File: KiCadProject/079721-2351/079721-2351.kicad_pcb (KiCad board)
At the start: 2 copper layers, 159.3 x 154.2 mm, 241 parts, among them IC1 HC244, IC101 uPC177C, IC201 MP493, IC401 D151811-0360, IC402 IS157, IC501 D151821-0020, IC601 MP5273, IC602 TC4071BP_2, IC603 TC4069UPB_2, J201 Connected, J44 Conn_02x11_0x13_Top_Bottom_Sh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, J601 Connected, J711 Empty, Q802 C945, T1 2SB1015B, T211 RN1006, T711 2CS2001, T712 2SD1415, T721 2CS2001, T722 2SD1415, T751 CE1A3Q, T761 CE1A3Q, T801 2CS2001, T803 2CS4065, T811 2CS2001, T812 CE1A3Q, T821 Empty, T822 CE1A3Q (empty), T831 Empty, T832 CE1A3Q (empty), T841 2CS2001, T842 CE1A3Q, T851 Empty, T852 CE1A3Q (empty), T861 Empty, T911 RN1006, T921 RN1006, T921A1 Conn_01x01_Female, T921B1 Conn_01x01_Female, X601 Crystal

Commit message: Cleanup
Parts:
- removed IC602: TC4071BP_2, 40xx:40xx-DIL14
- removed IC603: TC4069UPB_2, 40xx:40xx-DIL14
- removed T712, T722: 2SD1415, 079721-2351:TO-220-3_Vertical_Mazda
- added T712A1: 2SD1415, 079721-2351:TO-220-3_Vertical_Mazda, F.Cu at (109.7, 29.0)
- added T722A1: 2SD1415, 079721-2351:TO-220-3_Vertical_Mazda, F.Cu at (125.5, 29.0)
- added U1: 4071, 40xx:40xx-DIL14, F.Cu at (216.9, 69.5)
- added U2: 4069, 40xx:40xx-DIL14, F.Cu at (201.2, 69.5)
- R602: value R_Network08_US_mazda -> R
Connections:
- net C711_2 renamed Net-(C711-Pad2)
- net C721_2 renamed Net-(C721-Pad1)
- net IC402_3 renamed IC601_41
- net IC602_13 renamed IC601_38
- net IC602_8 renamed IC601_37
- net IC603_5 renamed IC601_28
- net J19 renamed IC601_6
- net J23 renamed IC601_7
- net Net-(IC101-Pad1) renamed IC601_11
- net Net-(IC201-Pad17) renamed IC201_17
- net Net-(IC201-Pad18) renamed IC201_18
- net Net-(IC201-Pad19) renamed IC201_19
- net Net-(IC401-Pad21) renamed IC601_34
- net Net-(IC401-Pad22) renamed IC601_33
- net Net-(IC401-Pad23) renamed IC601_32
- net Net-(IC501-Pad10) renamed IC601_16
- net Net-(IC501-Pad4) renamed IC601_14
- net Net-(IC501-Pad5) renamed IC601_15
- net Net-(IC501-Pad6) renamed IC601_12
- net Net-(IC601-Pad19) renamed IC601_19
- net Net-(IC601-Pad29) renamed IC601_29
- net Net-(IC601-Pad40) renamed IC601_40
- net Net-(IC601-Pad42) renamed IC601_42
- net T211_2 renamed IC601_8
- net T711_2 renamed Net-(R711-Pad1)
- net T721_2 renamed Net-(R721-Pad1)
- net T861_10 renamed IC601_10
- net T861_3 renamed IC601_5
- net T861_9 renamed IC601_9
- IC601 pad 13: T861_13 -> IC601_13
- IC601 pad 17: T861_17 -> IC601_17
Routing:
- net T861_17: track 74.9 -> 0.00 mm
- net IC601_17: track 0.00 -> 74.9 mm
- net T861_13: track 58.7 -> 0.00 mm
- net IC601_13: track 0.00 -> 58.7 mm

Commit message: Cleanup
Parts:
- T811: value 2CS2001 -> 2SC1815
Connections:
- net C504 renamed Net-(C504-Pad2)
- net IC101_11 renamed Net-(IC101-Pad11)
- net IC101_4 renamed Net-(IC101-Pad4)
- net IC101_7 renamed Net-(C503-Pad2)
- net IC1_5 renamed IC601_1
- net J22 renamed Net-(T851-Pad3)
- net Q802_2 renamed Net-(Q802-Pad2)
- net T211_3 renamed Net-(D211-Pad1)
- net T801_2 renamed Net-(R801-Pad1)
- net T803_1 renamed Net-(Q802-Pad1)
- net T803_3 renamed Net-(R804-Pad1)
- net T811_2 renamed Net-(R811-Pad1)
- net T812_2 renamed Net-(D812-Pad2)
- net T821_2 renamed Net-(R821-Pad1)
- net T831_2 renamed Net-(R831-Pad1)
- net T841_2 renamed Net-(R841-Pad1)
- net T842_2 renamed Net-(R842-Pad1)
- net T842_3 renamed Net-(R841-Pad2)
- net T851_2 renamed Net-(R851-Pad1)
- net T852_2 renamed Net-(D851-Pad2)
- net T852_3 renamed Net-(R851-Pad2)
- net T861_2 renamed Net-(R861-Pad1)
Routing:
- net Net-(Q802-Pad1): track 54.1 -> 55.3 mm
- net IC601_2: track 82.2 -> 83.3 mm

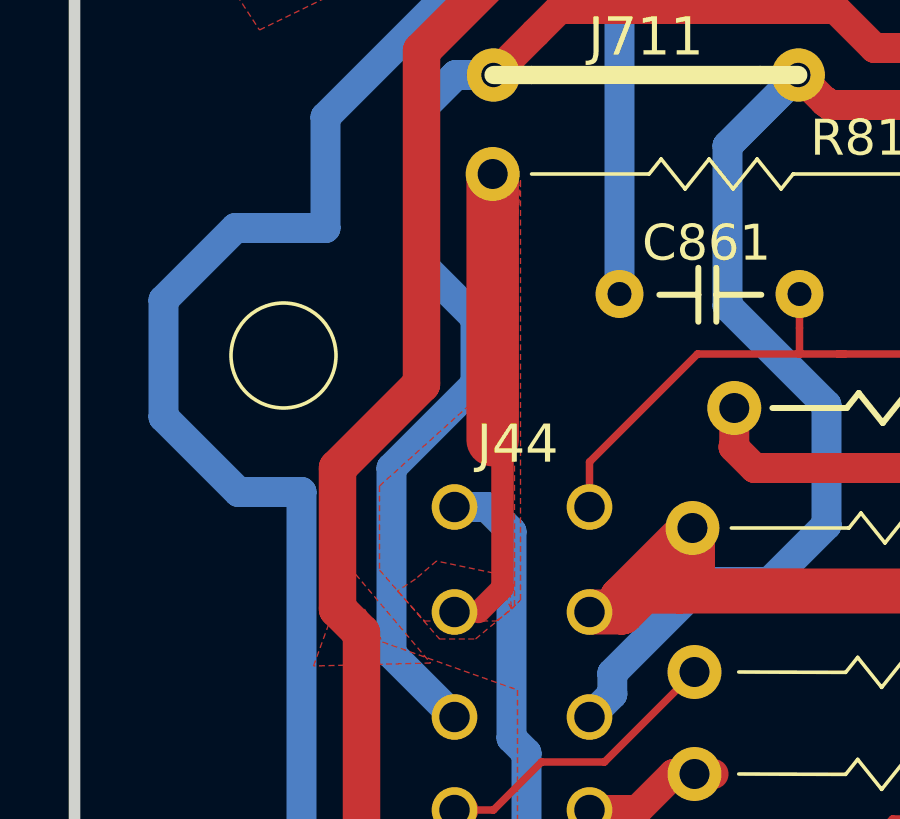
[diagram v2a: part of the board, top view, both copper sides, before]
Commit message: Input description TODO: Correct transistors pins
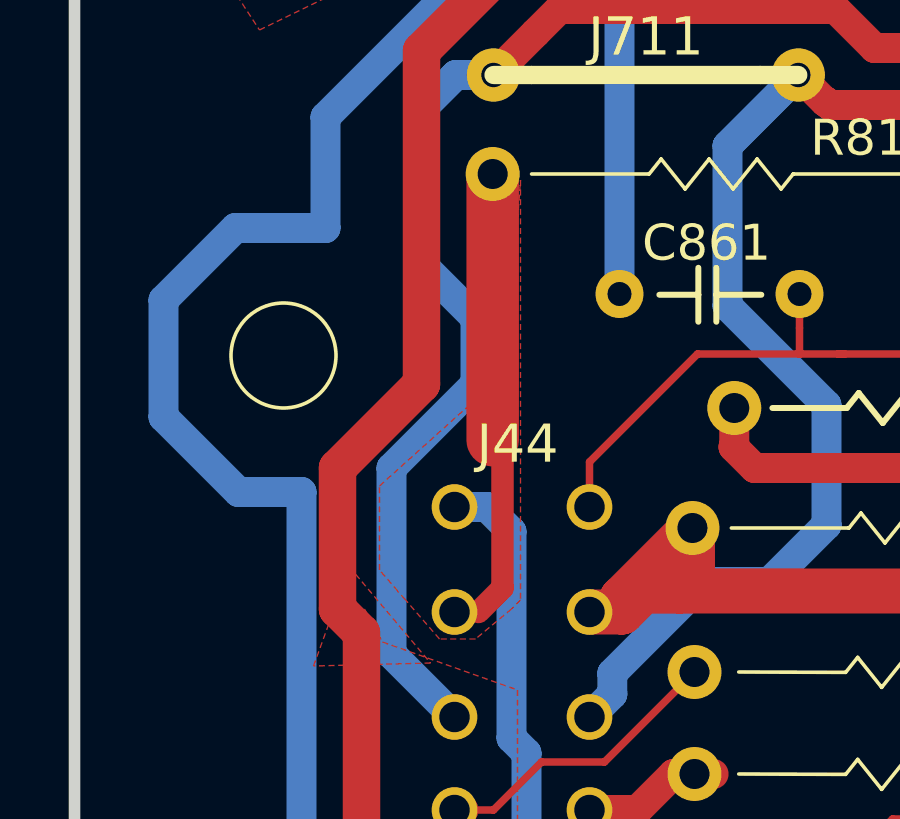
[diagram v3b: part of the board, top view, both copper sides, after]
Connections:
- net 2E renamed Crank_angle_sensor_N_CPK
- net 2G renamed Crank_angle_sensor_G_CMP
- net 2H renamed Fuel_pressure_regulator_solenoid_high_temp
- net 2I renamed Igniter_E
- net 2J renamed Radiator_fun_temperature_sensor
- net 2K renamed Airflow_meter_5V
- net 2L renamed Throttle_wide_open_sensor
- net 2M renamed Throttle_position_sensor
- net 2N renamed Oxygen_sensor
- net 2O renamed Volume_airflow_sensor
- net 2P renamed Airflow_meter_intake_air_thermosensor
- net 2Q renamed R432
- net 2U renamed Injectors_1_3
- net 2V renamed Injectors_2_4
- net 2W renamed Idle_air_control_valve
- net 2X renamed EVAP_canister_purage_valve
- net 2Z renamed Transsmision_control_module
- net A renamed +BATT
- net C renamed Starter_motor
- net D renamed Self_diagnostic_checker_monitor_lamp
- net E renamed Check_engine_indicator
- net F renamed Self_diagnostic_checker_code_no
- net G renamed Ignition_amp_1&4
- net H renamed Ignition_amp_2&3
- net J renamed AC_relay
- net L renamed Vehicle_speed_sensor
- net N renamed Throttle_sensor_idle_terminal
- net O renamed Stoplight_switch
- net P renamed Power_steering_pressure_switch
- net Q renamed AC_switch
- net R renamed Radiator_temperature_switch
- net S renamed Blower_motor_switch
- net U renamed Headlight_switch
- net V renamed Neutral_or_clutch_switch
- C1 pad 2: GND -> GNDS
- C101 pad 1: GND -> GNDS
- C105 pad 1: GND -> GNDS
- C111 pad 2: GND -> GNDS
- C2 pad 2: GND -> GNDS
- C201 pad 1: GND -> GNDS
- C202 pad 1: GND -> GNDS
- C203 pad 1: GND -> GNDS
- C204 pad 1: GND -> GNDS
- C205 pad 1: GND -> GNDS
- C3 pad 2: GND -> GNDS
- C4 pad 2: GND -> GNDS
- C401 pad 1: GND -> GNDS
- C405 pad 2: GND -> GNDS
- C411 pad 2: GND -> GNDS
- C421 pad 1: GND -> GNDS
- C422 pad 2: GND -> GNDS
- C431 pad 1: GND -> GNDS
- C432 pad 2: GND -> GNDS
- C441 pad 1: GND -> GNDS
- C442 pad 1: GND -> GNDS
- C451 pad 2: GND -> GNDS
- C452 pad 2: GND -> GNDS
- C461 pad 1: GND -> GNDS
- C471 pad 2: GND -> GNDS
- C472 pad 1: GND -> GNDS
- C481 pad 1: GND -> GNDS
- C491 pad 1: GND -> GNDS
- C5 pad 2: GND -> GNDS
- C501 pad 1: GND -> GNDS
- C502 pad 1: GND -> GNDS
- C503 pad 1: GND -> GNDS
- C504 pad 1: GND -> GNDS
- C51 pad 1: GND -> GNDS
- C511 pad 2: GND -> GNDS
- C52 pad 2: GND -> GNDS
- C53 pad 1: GND -> GNDS
- C54 pad 1: GND -> GNDS
- C6 pad 2: GND -> GNDS
- C601 pad 1: GND -> GNDS
- C602 pad 1: GND -> GNDS
- C603 pad 1: GND -> GNDS
- C604 pad 2: GND -> GNDS
- C605 pad 2: GND -> GNDS
- C606 pad 1: GND -> GNDS
- C607 pad 2: GND -> GNDS
- C7 pad 2: GND -> GNDS
- C8 pad 2: GND -> GNDS
- C801 pad 2: 2A -> GND
- C861 pad 2: GND -> GNDS
- C911 pad 2: GND -> GNDS
- C921 pad 2: GND -> GNDS
- D2 pad 2: GND -> GNDS
- D4 pad 2: GND -> GNDS
- D5 pad 2: GND -> GNDS
- D901 pad 1: 2A -> GND
- D901 pad 2: GND -> GNDS
- F401 pad 2: GND -> GNDS
- GND1 pad 1: GND -> GNDS
- IC1 pad 10: GND -> GNDS
- IC1 pad 9: GND -> GNDS
- IC101 pad 12: GND -> GNDS
- IC201 pad 12: GND -> GNDS
- IC401 pad 18: GND -> GNDS
- IC401 pad 25: GND -> GNDS
- IC401 pad 27: GND -> GNDS
- IC401 pad 28: GND -> GNDS
- IC402 pad 5: GND -> GNDS
- IC501 pad 12: GND -> GNDS
- IC601 pad 23: GND -> GNDS
- J201 pad 2: GND -> GNDS
- J44 pad 2A: 2A -> GND
- J44 pad 2B: 2A -> GND
- J44 pad 2C: GND -> GNDS
- J44 pad 2D: GND -> GNDS
- R104 pad 1: GND -> GNDS
- R114 pad 2: GND -> GNDS
- R401 pad 2: GND -> GNDS
- R412 pad 2: GND -> GNDS
- R451 pad 2: GND -> GNDS
- R463 pad 2: GND -> GNDS
- R483 pad 1: GND -> GNDS
- R493 pad 2: GND -> GNDS
- R502 pad 1: GND -> GNDS
- R507 pad 1: GND -> GNDS
- R508 pad 1: GND -> GNDS
- R509 pad 1: GND -> GNDS
- R562 pad 1: GND -> GNDS
- R712 pad 1: 2A -> GND
- R713 pad 2: 2A -> GND
- R722 pad 2: 2A -> GND
- R723 pad 2: 2A -> GND
- R805 pad 2: 2A -> GND
- T211 pad 1: GND -> GNDS
- T712A1 pad 3: 2A -> GND
- T722A1 pad 3: 2A -> GND
- T751 pad 1: GND -> GNDS
- T761 pad 1: GND -> GNDS
- T812 pad 1: 2A -> GND
- T822 pad 1: 2A -> GND
- T832 pad 1: 2A -> GND
- T842 pad 1: 2A -> GND
- T852 pad 1: 2A -> GND
- T861 pad 1: GND -> GNDS
- T911 pad 1: GND -> GNDS
- T921 pad 1: GND -> GNDS
- T921A1 pad 1: 2A -> GND
- U1 pad 7: GND -> GNDS
- U2 pad 7: GND -> GNDS
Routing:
- net GNDS: track 0.00 -> 1878.4 mm, vias 0 -> 11
- net GND: track 1878.4 -> 314.8 mm, vias 11 -> 1
- net 2A: track 314.8 -> 0.00 mm, vias 1 -> 0
- added copper zone on B.Cu, net GNDS
- added copper zone on F.Cu, net GNDS
- removed copper zone on B.Cu, net GND
- removed copper zone on F.Cu, net GND

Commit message: Cleanup
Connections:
- net IC402_24 renamed IC401_24
- net Net-(C491-Pad2) renamed IC401_19
- net Vehicle_speed_sensor renamed Transsmision_control_module_2

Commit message: Cleanup
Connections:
- net C501_2 renamed /IC501_20
- net C501_3 renamed /IC501_19
- net C501_5 renamed /IC501_17
- net C501_7 renamed /IC501_14
- net C502_7 renamed /IC501_13
- net IC101_2 renamed IC401_6
- net IC1_4 renamed +5V
- net IC201_15 renamed /IC201_15
- net IC201_16 renamed /IC201_16
- net IC201_18 renamed /IC201_18
- net IC201_19 renamed /IC201_19
- net IC401_19 renamed /IC401_19
- net IC402_4 renamed IC401_4
- net IC501_21 renamed /IC501_21
- net IC501_22 renamed /IC501_22
- net IC601_13 renamed /IC601_13
- net IC601_17 renamed /IC601_17
- net IC601_2 renamed /IC601_2
- net IC601_3 renamed /IC601_3
- net IC601_30 renamed /IC601_30
- net IC601_35 renamed /IC601_35
- net IC601_4 renamed /IC601_4
- net IC601_9 renamed /IC601_9
- net IC602_9 renamed Net-(U1-Pad12)
- net Net-(C201-Pad2) renamed /IC201_8
- net Net-(C202-Pad2) renamed /IC201_9
- net Net-(C203-Pad2) renamed /IC201_10
- net Net-(C204-Pad2) renamed /IC201_11
- net Net-(C401-Pad2) renamed /IC401_14
- net Net-(C422-Pad1) renamed /IC401_12
- net Net-(C432-Pad1) renamed /IC401_11
- net Net-(C442-Pad2) renamed /IC401_10
- net Net-(C452-Pad1) renamed /IC401_9
- net Net-(C472-Pad2) renamed /IC401_7
- net Net-(C481-Pad2) renamed /IC401_1
- net Net-(C501-Pad4) renamed /IC501_18
- net Net-(C501-Pad6) renamed /IC501_15
- net Net-(C502-Pad5) renamed /IC501_16
- net Net-(IC201-Pad4) renamed IC201_4
- net Net-(IC201-Pad7) renamed IC201_7
- net Net-(IC401-Pad13) renamed /IC401_13
- net Net-(IC601-Pad20) renamed /IC601_20
- net R412 renamed Net-(R411-Pad2)
- net R414 renamed Net-(C411-Pad1)
- net R432 renamed Water_thermosensor
- net R461_1 renamed /IC401_8
- IC401 pad 2: IC402_2 -> IC401_2
- IC402 pad 7: Net-(IC402-Pad7) -> IC402_2
- IC501 pad 7: IC402_2 -> IC401_2
- R461 pad 2: Net-(IC402-Pad7) -> IC402_2
- R462 pad 1: Net-(IC402-Pad7) -> IC402_2
- R463 pad 1: Net-(IC402-Pad7) -> IC402_2
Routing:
- net IC401_2: track 0.00 -> 99.3 mm, vias 0 -> 1
- net Net-(IC402-Pad7): track 63.6 -> 0.00 mm
- net IC402_2: track 99.3 -> 63.6 mm, vias 1 -> 0

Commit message: Cleanup
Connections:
- net IC401_6 renamed /IC401_6
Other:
- board text added: "Holes positions PCB shape"
- board text added: "TODO"

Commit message: cleanup
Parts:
- T1: footprint 079721-2351:TO-220-3_Vertical_Mazda -> 079721-2351:2SB1015B
- T712: renamed from T712A1; footprint 079721-2351:TO-220-3_Vertical_Mazda -> 079721-2351:2SD1415
- T722: renamed from T722A1; footprint 079721-2351:TO-220-3_Vertical_Mazda -> 079721-2351:2SD1415
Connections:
- net IC1_6 renamed Net-(C3-Pad1)
- net IC402_2 renamed Net-(IC402-Pad7)
- net IC601_1 renamed /IC601_1
- net IC601_29 renamed /IC601_29
- IC1 pad 3: IC1_3 -> Net-(IC1-Pad3)
- T1 pad 1: IC1_3 -> +5V
- T1 pad 2: +5V -> Net-(IC1-Pad3)
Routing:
- net Net-(IC1-Pad3): track 0.00 -> 46.7 mm, vias 0 -> 1
- net IC1_3: track 46.7 -> 0.00 mm, vias 1 -> 0
- net Igniter_E: track 139.3 -> 135.7 mm
- net /IC201_16: track 61.6 -> 59.3 mm
- net /IC201_15: track 66.2 -> 64.0 mm
- net IC602_10: track 42.7 -> 41.2 mm
- net Net-(T851-Pad3): track 62.1 -> 60.8 mm
- net Net-(R851-Pad1): track 23.7 -> 22.6 mm
- net Net-(R711-Pad2): track 56.7 -> 57.4 mm
- net GNDS: track 1878.4 -> 1877.7 mm
- net IC602_11: track 48.5 -> 47.9 mm
- net Net-(R721-Pad2): track 29.7 -> 29.2 mm
